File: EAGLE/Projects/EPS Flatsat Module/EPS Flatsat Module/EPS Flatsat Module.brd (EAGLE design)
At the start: 100 x 80 mm, 2 parts, among them J1 ESQ-126-39-G-D, J2 ESQ-126-39-G-D

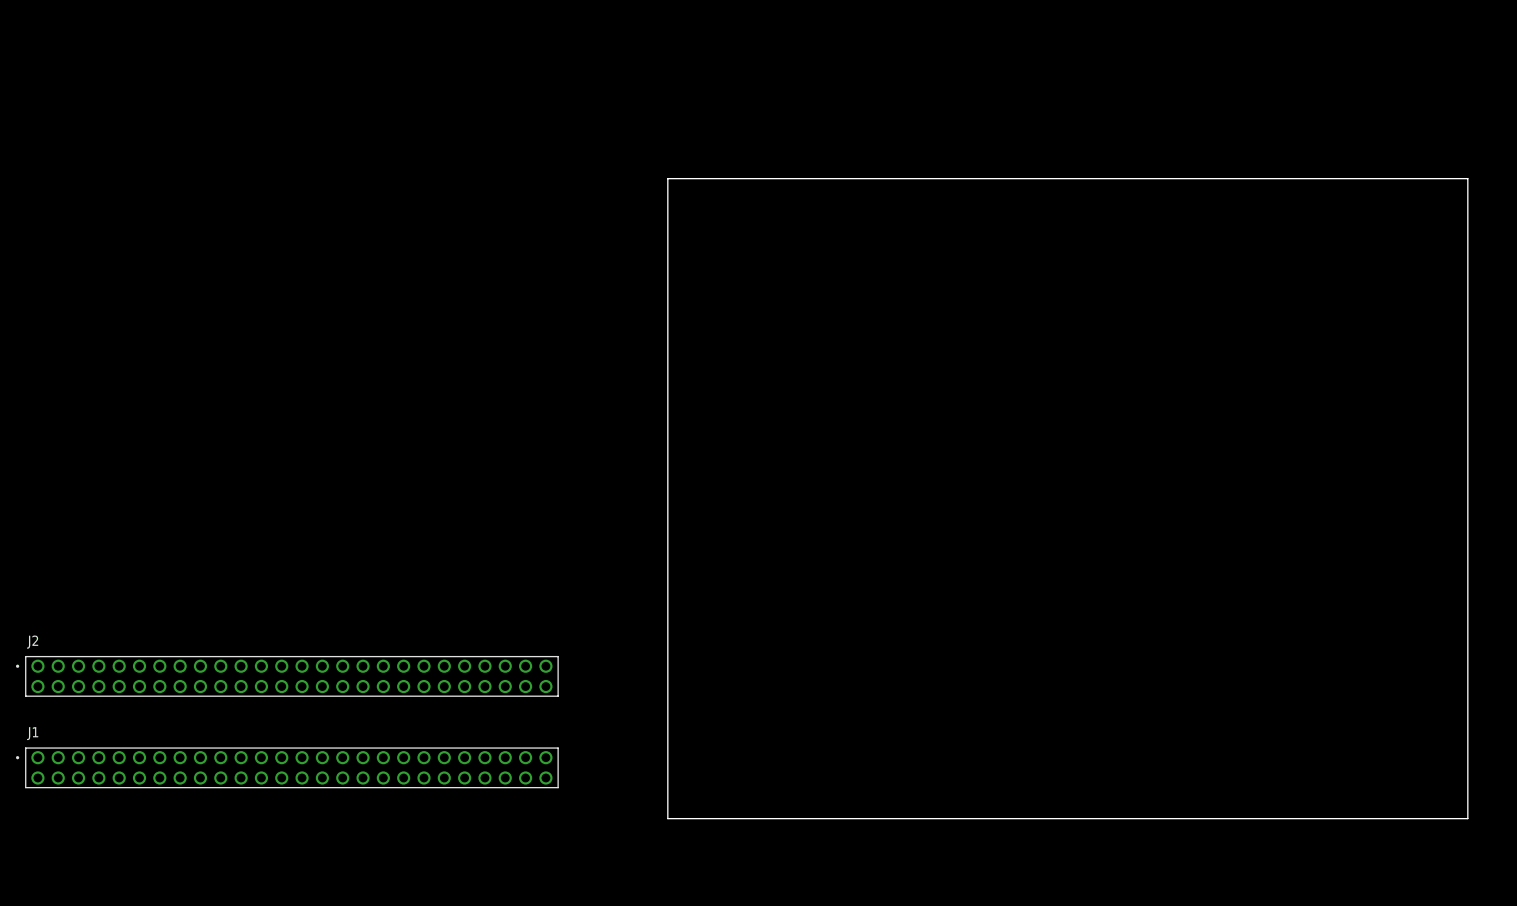
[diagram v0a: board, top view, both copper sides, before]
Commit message: Updates to flatsat module. Added MSP430 headers, DCDC converters, and some power switches to schematic. Did some placement on the board layout.
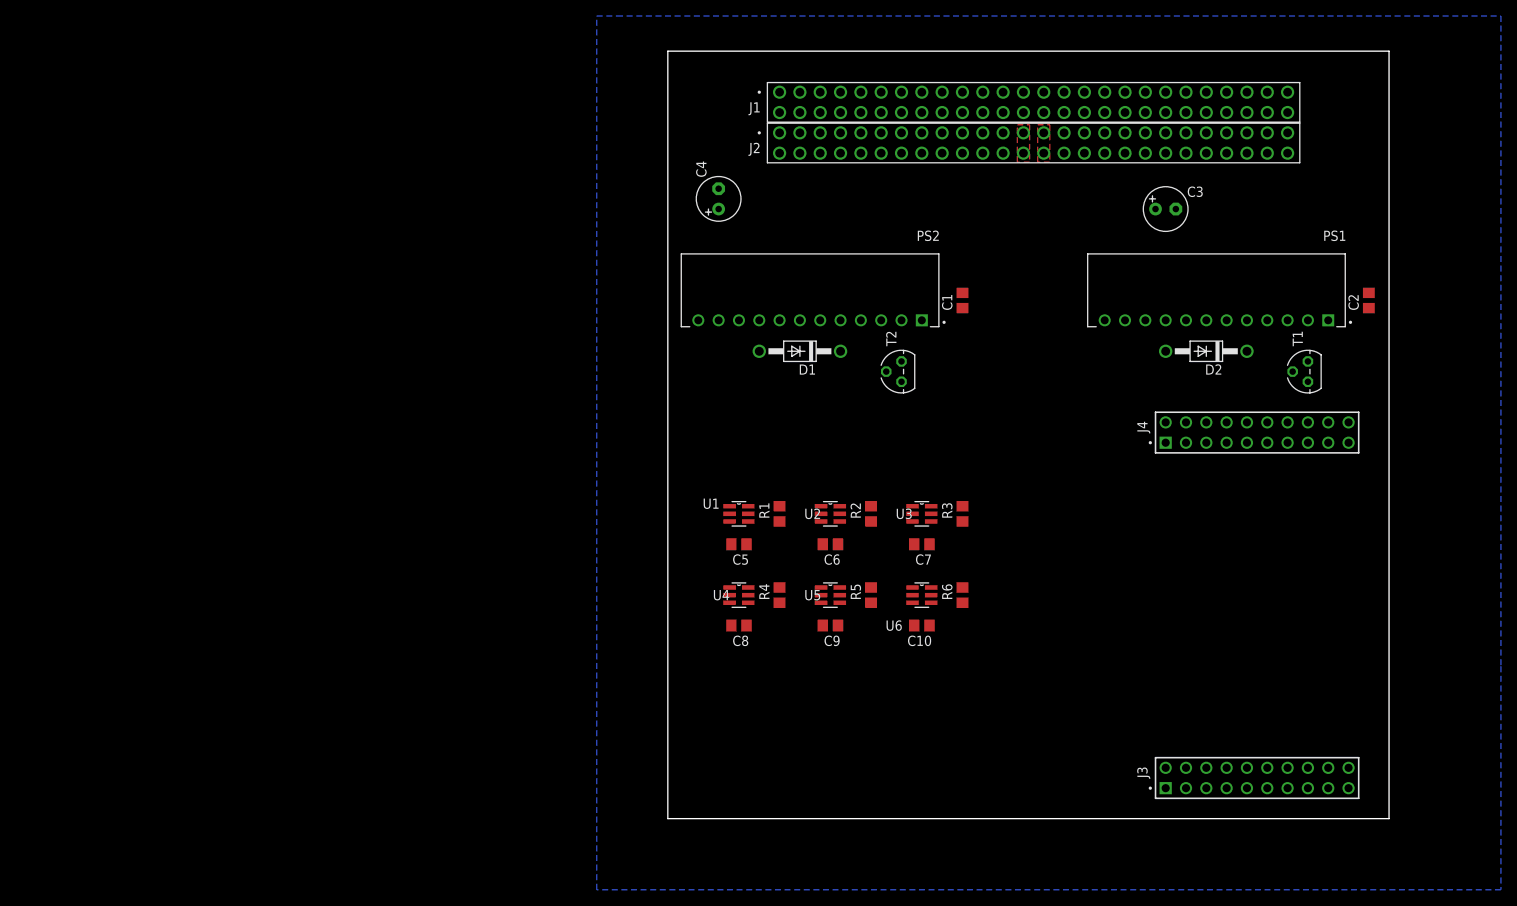
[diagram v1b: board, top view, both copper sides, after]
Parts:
- added C1, C2: (no value), rcl:C0805
- added C10, C5, C6, C7, C8, C9: 1u, rcl:C0805
- added C3, C4: (no value), rcl:E2,5-6
- added D1, D2: 1N4004, diode:DO41-10
- added J3, J4: TSW-110-23-F-D, TSW-110-23-F-D:SAMTEC_TSW-110-23-F-D
- added PS1: R-543.3PA, R-543.3PA:CONV_R-543.3PA
- added PS2: R-545.0PA, R-545.0PA:CONV_R-545.0PA
- added R1, R2, R3, R4, R5, R6: 10k, rcl:R0805
- added T1, T2: 2N3904, transistor:TO92
- added U1, U2, U3, U4, U5, U6: Value, TPS27081ADDCR:DDC0006A_N
- moved J1 124.6 mm to (14.0, 90.8)
- moved J2 114.2 mm to (14.0, 85.7)
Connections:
- new net 3V3ONOFF: T1.2
- new net 3V3SYS: C10.1, C3.+, C8.1, C9.1, D1.A, J2.27, J2.28, PS1.10, PS1.11, PS1.9, R4.1, R5.1, R6.1, U4.4, U5.4, U6.4
- new net 5VONOFF: T2.2
- new net 5VSYS: C4.+, C5.1, C6.1, C7.1, D2.A, J2.25, J2.26, PS2.10, PS2.11, PS2.9, R1.1, R2.1, R3.1, U1.4, U2.4, U3.4
- new net GND: C1.2, C10.2, C2.2, C3.-, C4.-, C5.2, C6.2, C7.2, C8.2, C9.2, J2.14, J2.17, J2.21, J2.22, J2.29, J2.30, J2.32, J2.47, J2.48, J2.9, J3.04, J4.02, PS1.5, PS1.6, PS1.7, PS1.8, PS2.5, PS2.6, PS2.7, PS2.8, T1.3, T2.3, U1.1, U2.1, U3.1, U4.1, U5.1, U6.1
- new net N$1: PS1.1, T1.1
- new net N$2: PS2.1, T2.1
- new net N$3: R1.2, U1.6
- new net N$4: R2.2, U2.6
- new net N$5: R3.2, U3.6
- new net N$6: R4.2, U4.6
- new net N$7: R5.2, U5.6
- new net N$8: R6.2, U6.6
- new net PDM10: J2.20, U6.2, U6.3
- new net PDM10EN: U6.5
- new net PDM5: J2.13, U1.2, U1.3
- new net PDM5EN: U1.5
- new net PDM6: J2.15, U2.2, U2.3
- new net PDM6EN: U2.5
- new net PDM7: J2.16, U3.2, U3.3
- new net PDM7EN: U3.5
- new net PDM8: J2.18, U4.2, U4.3
- new net PDM8EN: U4.5
- new net PDM9: J2.19, U5.2, U5.3
- new net PDM9EN: U5.5
- new net SCL: J1.43, J4.14
- new net SDA: J1.41, J4.12
- new net VIN: C1.1, C2.1, D1.C, D2.C, PS1.2, PS1.3, PS1.4, PS2.2, PS2.3, PS2.4
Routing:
- added copper zone on layer 1, net 3V3SYS
- added copper zone on layer 1, net 5VSYS
- added copper zone on layer 16, net GND
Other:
- board size 100 x 80 mm -> 90.2 x 95.9 mm
